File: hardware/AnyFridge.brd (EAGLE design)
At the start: 75.9 x 69.8 mm, 14 parts

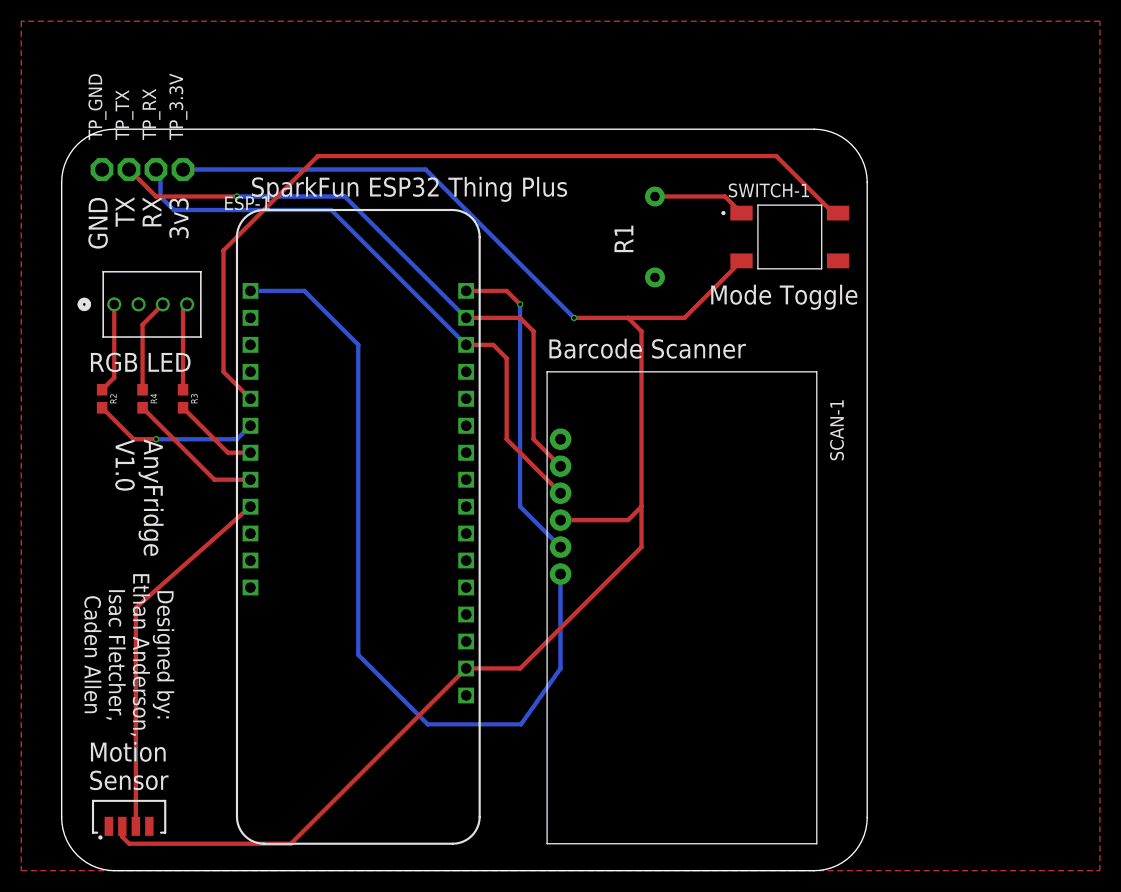
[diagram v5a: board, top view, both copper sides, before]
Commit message: Fix TX + RX on Scanner LIB + Flip Scanner on AnyFridgeBRD
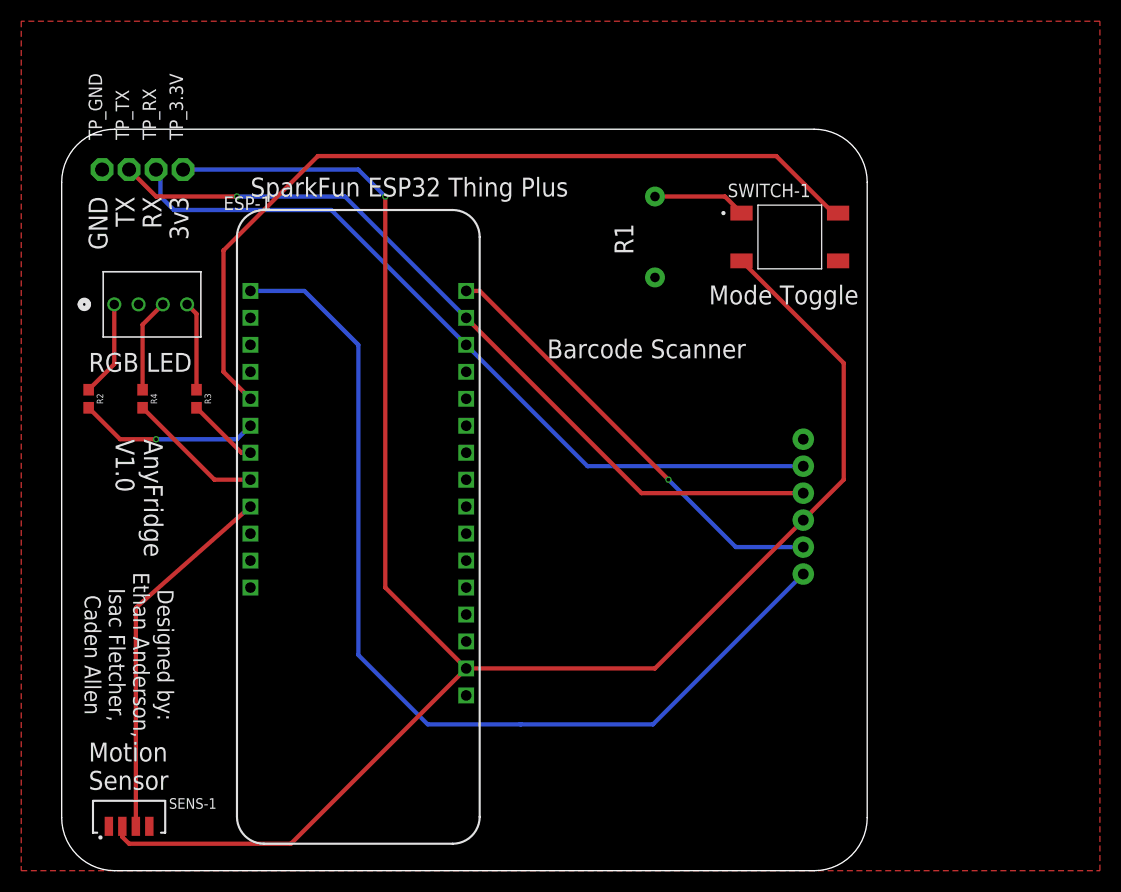
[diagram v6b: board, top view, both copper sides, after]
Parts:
- moved SCAN-1 25.4 mm to (48.3, 47.0), flipped to the bottom
- moved R2 1.27 mm to (5.08, 44.5)
- moved R3 1.27 mm to (15.2, 44.5)
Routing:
- net 3.3V: track 152.6 -> 175.7 mm
- net TX1: track 58.2 -> 76.1 mm
- net RX1: track 56.4 -> 73.8 mm
- net STAT: track 74.8 -> 92.0 mm
- net TRIG: track 30.0 -> 41.7 mm
- net RED: track 15.7 -> 17.0 mm
- net GREEN: track 8.10 -> 6.83 mm
- net RED-IN: track 8.51 -> 9.04 mm

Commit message: Add mounting holes
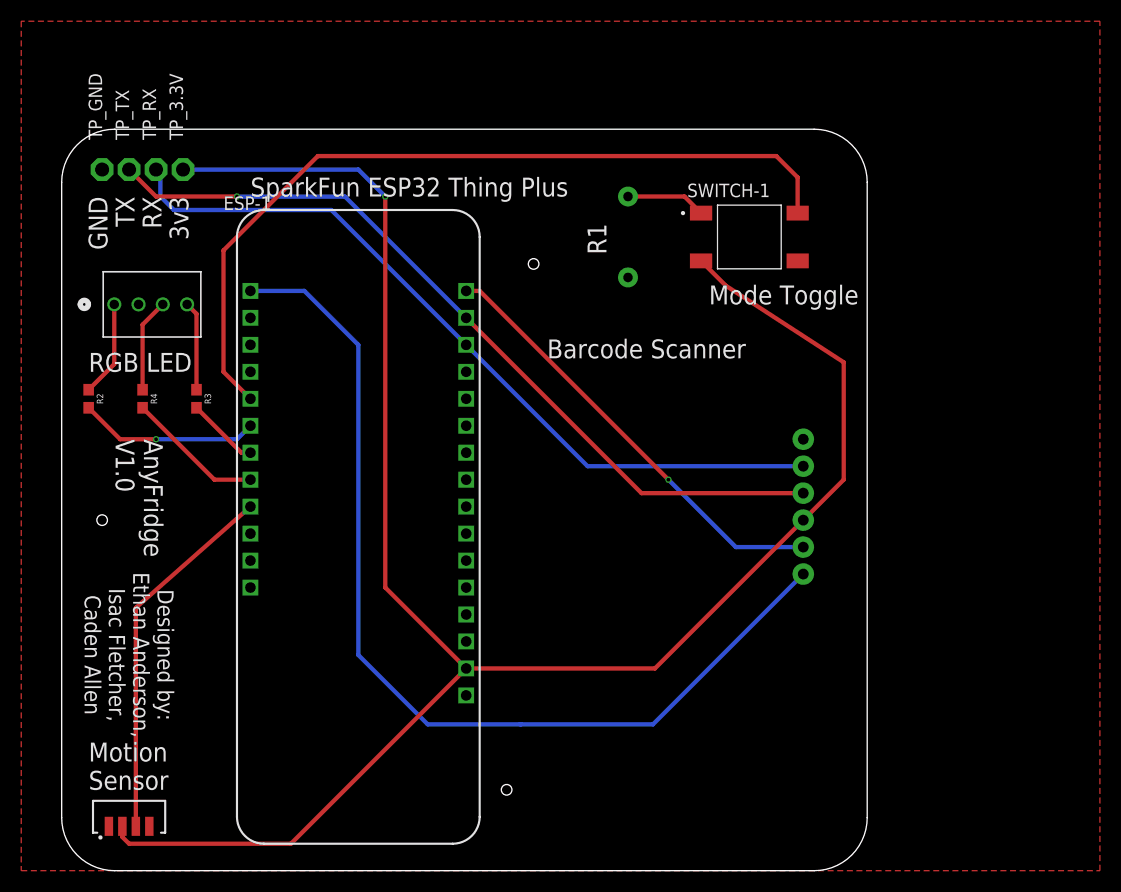
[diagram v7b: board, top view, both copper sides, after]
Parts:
- moved SWITCH-1 3.81 mm to (67.3, 59.7)
- moved R1 2.54 mm to (55.9, 59.7)
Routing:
- net 3.3V: track 175.7 -> 178.7 mm
- net SWI-OUT: track 78.8 -> 77.0 mm
- net N$1: track 8.80 -> 7.53 mm
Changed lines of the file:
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@@
 Isac Fletcher,
 Caden Allen</text>
-<text x="54.61" y="60.96" size="1.778" layer="21" rot="R270">R1</text>
+<text x="52.07" y="60.96" size="1.778" layer="21" rot="R270">R1</text>
 <text x="48.26" y="48.26" size="1.778" layer="21">Barcode Scanner</text>
 <text x="20.32" y="63.5" size="1.778" layer="21">SparkFun ESP32 Thing Plus</text>
@@
 <text x="7.62" y="40.64" size="1.778" layer="21" rot="SR270">AnyFridge
 V1.0</text>
+<hole x="44.45" y="7.62" drill="1"/>
+<hole x="46.99" y="57.15" drill="1"/>
+<hole x="6.35" y="33.02" drill="1"/>
 </plain>
 <attributes>
@@
 </class>
 </classes>
-<designrules name="oshpark-2layer">
+<designrules name="oshpark-2layer *">
 <description language="en">&lt;b&gt;OSH Park Design Rules&lt;/b&gt;
 &lt;p&gt;
@@
 <param name="mtCopper" value="0.035559375mm 0.0356mm 0.0356mm 0.0356mm 0.0356mm 0.0356mm 0.0356mm 0.0356mm 0.0356mm 0.0356mm 0.0356mm 0.0356mm 0.0356mm 0.0356mm 0.0356mm 0.035559375mm"/>
 <param name="mtIsolate" value="1.6mm 0.1499mm 0.2007mm 0.1499mm 0.2007mm 0.1499mm 0.2007mm 0.1499mm 0.2007mm 0.1499mm 0.2007mm 0.1499mm 0.2007mm 0.1499mm 0.2007mm"/>
-<param name="mdWireWire" value="6mil"/>
+<param name="mdWireWire" value="16mil"/>
 <param name="mdWirePad" value="6mil"/>
 <param name="mdWireVia" value="6mil"/>
@@
 <attribute name="VALUE" x="7.7978" y="57.785" size="1.27" layer="27" ratio="6" rot="SR0"/>
 </element>
-<element name="R1" library="SparkFun-Resistors" library_urn="urn:adsk.eagle:library:532" package="AXIAL-0.3" package3d_urn="urn:adsk.eagle:package:39658/2" value="10k" x="58.42" y="59.69" smashed="yes" rot="MR90">
-<attribute name="NAME" x="59.436" y="59.69" size="0.6096" layer="26" font="vector" ratio="20" rot="MR90" align="bottom-center"/>
-<attribute name="PROD_ID" value="RES-12183" x="-95.25" y="95.25" size="1.778" layer="28" rot="MR90" display="off"/>
-<attribute name="VALUE" x="57.404" y="59.69" size="0.6096" layer="28" font="vector" ratio="20" rot="MR90" align="top-center"/>
+<element name="R1" library="SparkFun-Resistors" library_urn="urn:adsk.eagle:library:532" package="AXIAL-0.3" package3d_urn="urn:adsk.eagle:package:39658/2" value="10k" x="55.88" y="59.69" smashed="yes" rot="MR90">
+<attribute name="NAME" x="56.896" y="59.69" size="0.6096" layer="26" font="vector" ratio="20" rot="MR90" align="bottom-center"/>
+<attribute name="PROD_ID" value="RES-12183" x="-97.79" y="95.25" size="1.778" layer="28" rot="MR90" display="off"/>
+<attribute name="VALUE" x="54.864" y="59.69" size="0.6096" layer="28" font="vector" ratio="20" rot="MR90" align="top-center"/>
 </element>
 <element name="SCAN-1" library="SEN-18088" package="SEN-18088" value="SEN-18088" x="48.26" y="46.99" smashed="yes" rot="MR270">
@@
 <attribute name="MF" value="Vishay" x="35.56" y="-148.59" size="1.778" layer="27" display="off"/>
 <attribute name="MP" value="TSSP77038TT" x="35.56" y="-148.59" size="1.778" layer="27" display="off"/>
+<attribute name="NAME" x="12.64" y="5.83" size="1" layer="25" ratio="20" rot="SR0"/>
 <attribute name="NAME" x="12.64" y="5.83" size="1" layer="51" ratio="21" rot="SR0"/>
-<attribute name="NAME" x="12.64" y="5.83" size="1" layer="25" ratio="20" rot="SR0"/>
 <attribute name="PACKAGE" value="None" x="35.56" y="-148.59" size="1.778" layer="27" display="off"/>
 <attribute name="PRICE" value="None" x="35.56" y="-148.59" size="1.778" layer="27" display="off"/>
@@
 <attribute name="VALUE" x="12.64" y="4.53" size="1" layer="27" ratio="20" rot="SR0"/>
 </element>
-<element name="SWITCH-1" library="MISC-PARTS" package="SW_TS04-66-73-BK-100-SMT" value="TS04-66-73-BK-100-SMT" x="71.12" y="59.69" smashed="yes">
-<attribute name="MANUFACTURER" value="CUI Devices" x="142.24" y="-60.96" size="1.778" layer="27" display="off"/>
-<attribute name="NAME" x="65.27" y="63.44" size="1.27" layer="25"/>
-<attribute name="PARTREV" value="1.0" x="142.24" y="-60.96" size="1.778" layer="27" display="off"/>
-<attribute name="STANDARD" value="Manufacturer Recommendations" x="142.24" y="-60.96" size="1.778" layer="27" display="off"/>
-<attribute name="VALUE" x="65.27" y="55.94" size="1.27" layer="27" align="top-left"/>
+<element name="SWITCH-1" library="MISC-PARTS" package="SW_TS04-66-73-BK-100-SMT" value="TS04-66-73-BK-100-SMT" x="67.31" y="59.69" smashed="yes">
+<attribute name="MANUFACTURER" value="CUI Devices" x="138.43" y="-60.96" size="1.778" layer="27" display="off"/>
+<attribute name="NAME" x="61.46" y="63.44" size="1.27" layer="25"/>
+<attribute name="PARTREV" value="1.0" x="138.43" y="-60.96" size="1.778" layer="27" display="off"/>
+<attribute name="STANDARD" value="Manufacturer Recommendations" x="138.43" y="-60.96" size="1.778" layer="27" display="off"/>
+<attribute name="VALUE" x="61.46" y="55.94" size="1.27" layer="27" align="top-left"/>
 </element>
 <element name="TP_GND" library="testpad" library_urn="urn:adsk.eagle:library:385" package="P1-13" package3d_urn="urn:adsk.eagle:package:27946/1" value="TPPAD1-13" x="6.35" y="66.04" smashed="yes" rot="R90">
@@
 <wire x1="33.02" y1="63.5" x2="30.48" y2="66.04" width="0.4064" layer="16"/>
 <wire x1="72.39" y1="33.02" x2="76.2" y2="36.83" width="0.4064" layer="1"/>
-<wire x1="76.2" y1="36.83" x2="76.2" y2="47.81" width="0.4064" layer="1"/>
-<wire x1="76.2" y1="47.81" x2="66.57" y2="57.44" width="0.4064" layer="1"/>
+<wire x1="76.2" y1="36.83" x2="76.2" y2="47.885065625" width="0.4064" layer="1"/>
+<wire x1="76.2" y1="47.885065625" x2="65.11395" y2="55.08605" width="0.4064" layer="1"/>
+<wire x1="65.11395" y1="55.08605" x2="62.76" y2="57.44" width="0.4064" layer="1"/>
 </signal>
 <signal name="TRIG">
@@
 <contactref element="SWITCH-1" pad="1"/>
 <contactref element="R1" pad="P$2"/>
-<wire x1="58.42" y1="63.5" x2="65.01" y2="63.5" width="0.4064" layer="1"/>
-<wire x1="65.01" y1="63.5" x2="66.57" y2="61.94" width="0.4064" layer="1"/>
+<wire x1="55.88" y1="63.5" x2="61.2" y2="63.5" width="0.4064" layer="1"/>
+<wire x1="61.2" y1="63.5" x2="62.76" y2="61.94" width="0.4064" layer="1"/>
 </signal>
 <signal name="TX1">
@@
 <wire x1="26.67" y1="67.31" x2="17.78" y2="58.42" width="0.4064" layer="1"/>
 <wire x1="17.78" y1="58.42" x2="17.78" y2="46.99" width="0.4064" layer="1"/>
-<wire x1="69.85" y1="67.31" x2="75.22" y2="61.94" width="0.4064" layer="1"/>
-<wire x1="75.22" y1="61.94" x2="75.67" y2="61.94" width="0.4064" layer="1"/>
+<wire x1="69.85" y1="67.31" x2="71.86" y2="65.3" width="0.4064" layer="1"/>
+<wire x1="71.86" y1="65.3" x2="71.86" y2="61.94" width="0.4064" layer="1"/>
 </signal>
 <signal name="SENS-OUT">
